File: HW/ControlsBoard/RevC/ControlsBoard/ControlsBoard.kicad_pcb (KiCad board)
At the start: 2 copper layers, 54.6 x 20.3 mm, 12 parts, among them J1 Conn_02x06_Odd_Even, SW1 Rotary_Encoder_Switch, SW2 SW_SPST, SW3 SW_SPST, SW4 SW_SPST, SW5 SW_SPST

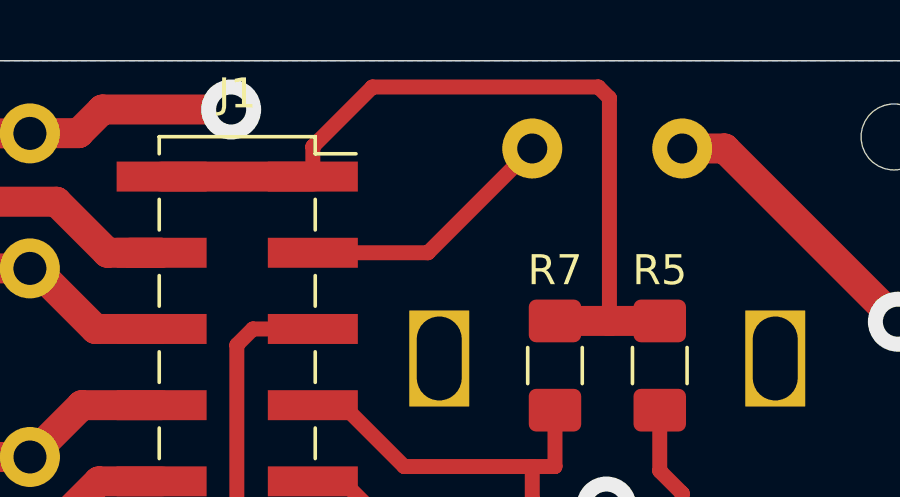
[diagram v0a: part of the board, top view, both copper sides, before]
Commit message: Created RevC - MainBoard and ControlBoard
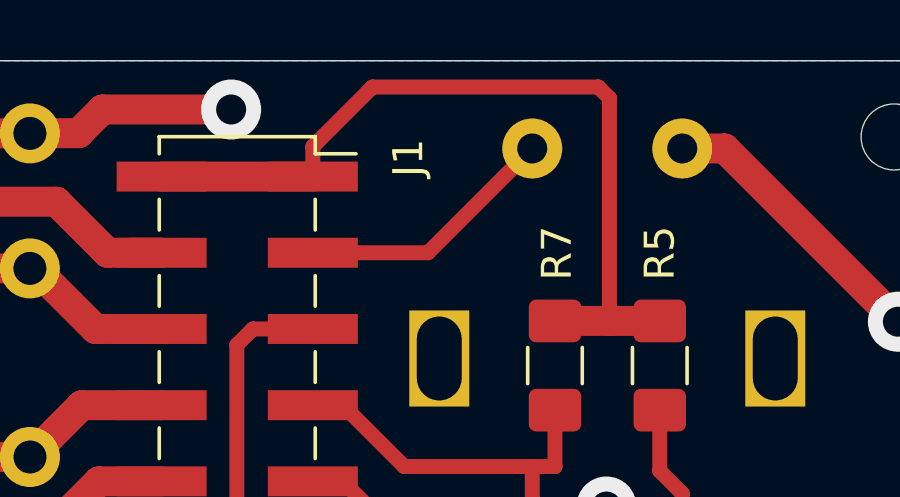
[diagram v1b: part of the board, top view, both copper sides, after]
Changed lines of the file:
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@@
     (tags "Surface mounted socket strip SMD 2x06 2.54mm double row")
     (attr smd)
-    (fp_text reference J1 (at 0 -9.12) (layer F.SilkS)
+    (fp_text reference J1 (at 5.7023 -6.9723 270) (layer F.SilkS)
       (effects (font (size 1 1) (thickness 0.15)))
     )
@@
     (descr https://www.omron.com/ecb/products/pdf/en-b3f.pdf)
     (tags "tact sw push 6mm")
-    (fp_text reference SW5 (at 3.25 2) (layer B.SilkS)
+    (fp_text reference SW5 (at -2.921 -4.191 90) (layer B.SilkS)
       (effects (font (size 1 1) (thickness 0.15)) (justify mirror))
     )
@@
     (descr https://www.omron.com/ecb/products/pdf/en-b3f.pdf)
     (tags "tact sw push 6mm")
-    (fp_text reference SW4 (at 3.25 2) (layer B.SilkS)
+    (fp_text reference SW4 (at -2.8956 -2.286 90) (layer B.SilkS)
       (effects (font (size 1 1) (thickness 0.15)) (justify mirror))
     )
@@
     (descr https://www.omron.com/ecb/products/pdf/en-b3f.pdf)
     (tags "tact sw push 6mm")
-    (fp_text reference SW3 (at 3.25 2) (layer B.SilkS)
+    (fp_text reference SW3 (at 9.271 -2.3495 90) (layer B.SilkS)
       (effects (font (size 1 1) (thickness 0.15)) (justify mirror))
     )
@@
     (descr https://www.omron.com/ecb/products/pdf/en-b3f.pdf)
     (tags "tact sw push 6mm")
-    (fp_text reference SW2 (at 3.25 2) (layer B.SilkS)
+    (fp_text reference SW2 (at 9.4615 -3.81 90) (layer B.SilkS)
       (effects (font (size 1 1) (thickness 0.15)) (justify mirror))
     )
@@
     (tags "resistor handsolder")
     (attr smd)
-    (fp_text reference R7 (at -3.175 0) (layer F.SilkS)
+    (fp_text reference R7 (at -3.7465 -0.0635 90) (layer F.SilkS)
       (effects (font (size 1 1) (thickness 0.15)))
     )
@@
     (tags "resistor handsolder")
     (attr smd)
-    (fp_text reference R5 (at -3.175 0) (layer F.SilkS)
+    (fp_text reference R5 (at -3.7465 0 90) (layer F.SilkS)
       (effects (font (size 1 1) (thickness 0.15)))
     )
@@
     (descr "Alps rotary encoder, EC12E... with switch, vertical shaft, http://www.alps.com/prod/info/E/HTML/Encoder/Incremental/EC11/EC11E15204A3.html")
     (tags "rotary encoder")
-    (fp_text reference SW1 (at 16.637 -8.128) (layer B.SilkS)
-      (effects (font (size 1 1) (thickness 0.15)) (justify mirror))
-    )
+    (fp_text reference SW1 (at 2.7559 4.6482 90) (layer B.SilkS)
+      (effects (font (size 1 1) (thickness 0.15)) (justify mirror))
+    )

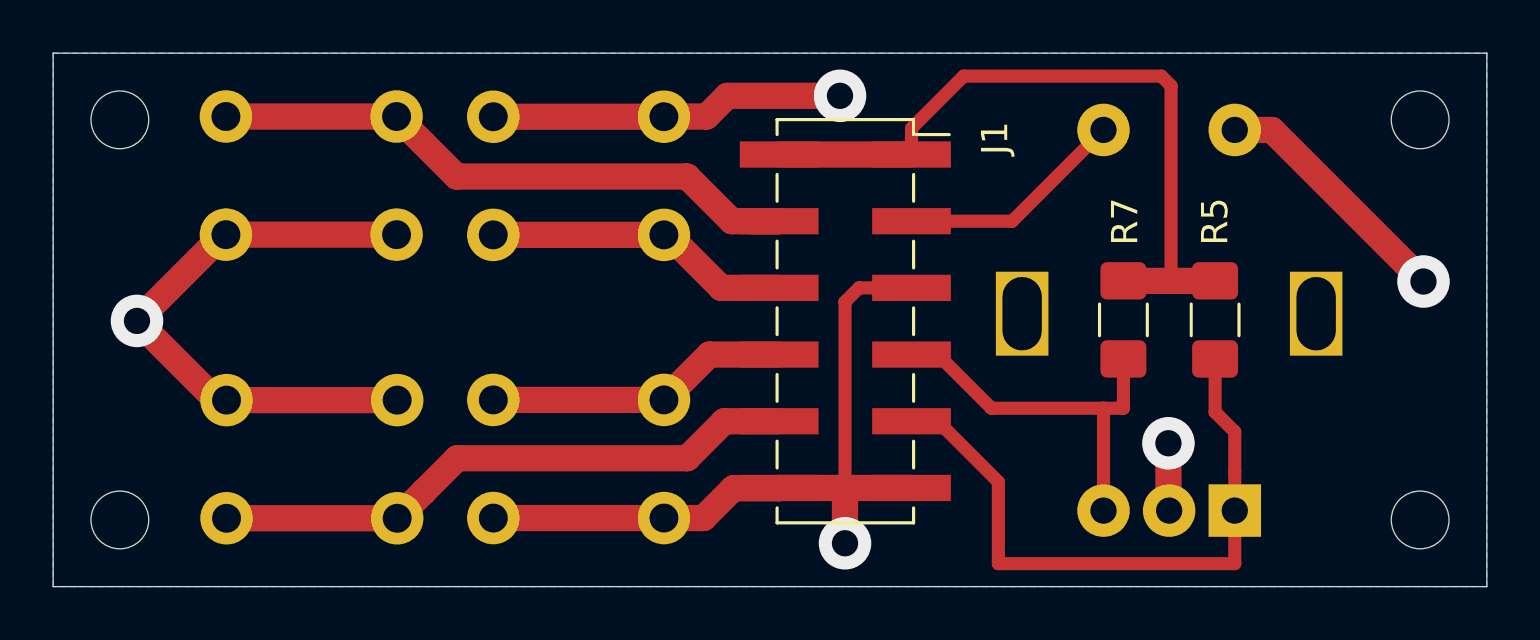
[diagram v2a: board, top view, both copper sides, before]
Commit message: updated front panel svg
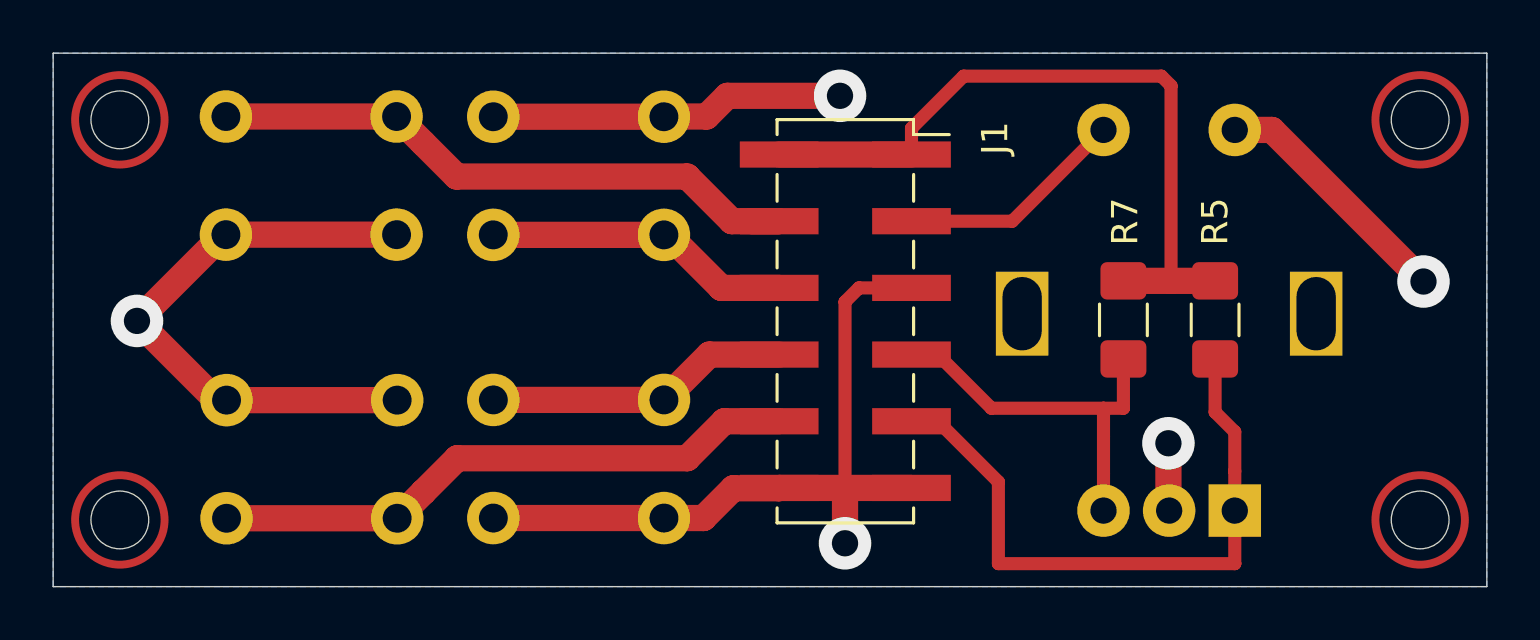
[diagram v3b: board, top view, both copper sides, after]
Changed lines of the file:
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@@
-(kicad_pcb (version 20171130) (host pcbnew "(5.1.5-0-10_14)")
+(kicad_pcb (version 20171130) (host pcbnew 5.1.5-52549c5~86~ubuntu18.04.1)
   (general
     (thickness 1.6)
-    (drawings 4)
+    (drawings 8)
     (tracks 79)
     (zones 0)
@@
     )
   )
+  (gr_circle (center 116.84 53.34) (end 118.543884 53.34) (layer F.Cu) (width 0.3))
+  (gr_circle (center 116.84 68.58) (end 118.543884 68.58) (layer F.Cu) (width 0.3))
+  (gr_circle (center 166.37 68.58) (end 168.073884 68.58) (layer F.Cu) (width 0.3))
+  (gr_circle (center 166.37 53.34) (end 168.073884 53.34) (layer F.Cu) (width 0.3))
   (gr_line (start 114.3 71.12) (end 114.3 50.8) (layer Edge.Cuts) (width 0.05))
   (gr_line (start 168.91 71.12) (end 114.3 71.12) (layer Edge.Cuts) (width 0.05))
